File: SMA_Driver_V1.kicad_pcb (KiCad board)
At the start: 2 copper layers, 93 x 93 mm, 74 parts, among them J1 Human_Interface_Tether, J2 RM08V_Conn, Q1 Q_NMOS_GDS, Q2 Q_NMOS_GDS, U1 UDT020A0X3-SRZ, U2 INA332, U3 MCP3208, U4 MicroSD_Breakout_ADF

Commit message: fixed notes on 'SMA Driver V1 changes for V2'
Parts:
- Q1, Q2: footprint custom:SO-8FL -> custom:SO-8FL_v2
- moved TP6 19.6 mm to (79.4, 31.0)
- moved TP4 18.0 mm to (34.9, 31.0)
- moved TP15 7.52 mm to (62.9, 33.5)
- moved R3 6.88 mm to (57.1, 33.5)
- moved R8 6.69 mm to (54.6, 33.5)
- moved TP18 6.69 mm to (48.9, 33.5)
- moved Q1 1.69 mm to (69.2, 29.1), turned to 0 degrees
- moved Q2 1.53 mm to (42.5, 28.4), turned to 0 degrees
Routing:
- net /SMA1_G: track 18.5 -> 0.00 mm, vias 1 -> 0
- net /SMA2_G: track 10.1 -> 0.00 mm, vias 1 -> 0
- net GND: track 131.4 -> 122.9 mm
- net /SMA_COM2: track 67.8 -> 59.6 mm, vias 4 -> 2
- net /SMA_COM1: track 65.5 -> 58.3 mm
- net /V_SMA1_-: track 0.00 -> 1.19 mm
- net /V_SMA2_-: track 0.00 -> 0.51 mm
- removed copper zone on B.Cu, net /V_SMA1_-
- removed copper zone on B.Cu, net /V_SMA2_-

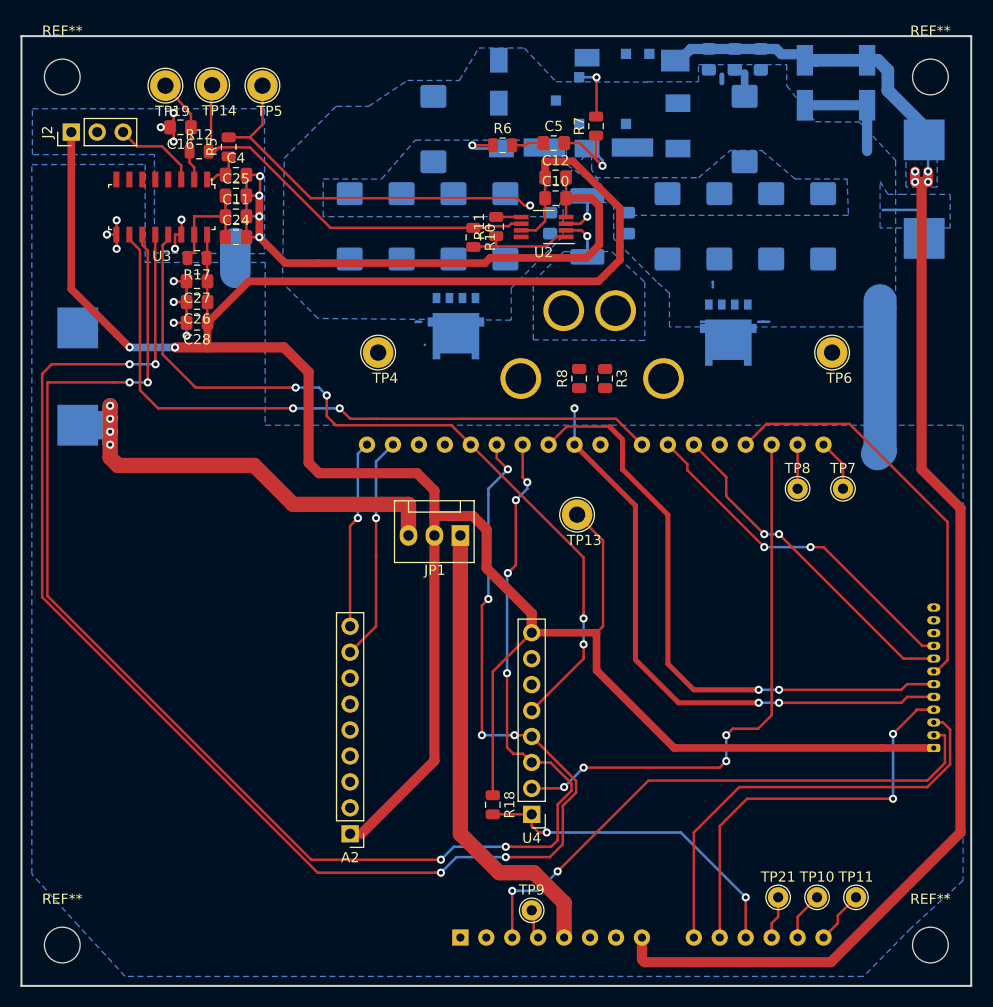
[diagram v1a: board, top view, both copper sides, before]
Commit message: PCB Rev 2.0 Fixed issues on PCB changes for V2 doc
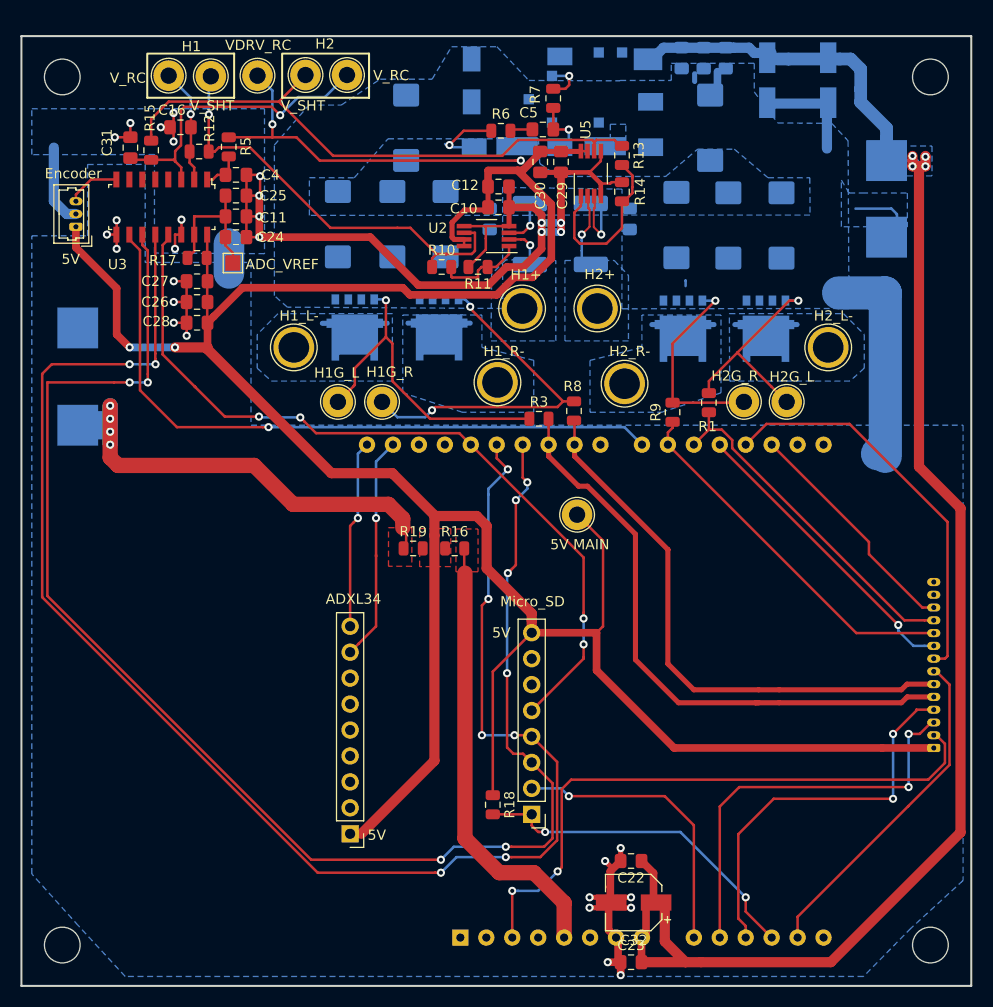
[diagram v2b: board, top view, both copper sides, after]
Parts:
- removed JP1: Jumper_NC_Dual, Connector:FanPinHeader_1x03_P2.54mm_Vertical
- removed TP9: 3V3, TestPoint:TestPoint_THTPad_D2.0mm_Drill1.0mm
- added C29: 100n, Capacitor_SMD:C_0805_2012Metric_Pad1.15x1.40mm_HandSolder, F.Cu at (52.8, 12.3)
- added C30: 4.7u, Capacitor_SMD:C_0805_2012Metric_Pad1.15x1.40mm_HandSolder, F.Cu at (50.8, 12.3)
- added C31: 1uF, Capacitor_SMD:C_0805_2012Metric_Pad1.15x1.40mm_HandSolder, F.Cu at (10.7, 10.9)
- added C32: 10uF, Capacitor_SMD:CP_Elec_5x5.3, F.Cu at (59.9, 84.8)
- added Q3: Q_NMOS_GDS, custom:SO-8FL_v2, B.Cu at (72.9, 28.7)
- added Q4: Q_NMOS_GDS, custom:SO-8FL_v2, B.Cu at (64.8, 28.7)
- added R1: 125, Resistor_SMD:R_0805_2012Metric, F.Cu at (67.3, 35.9)
- added R13: 24k, Resistor_SMD:R_0805_2012Metric, F.Cu at (58.8, 11.7)
- added R14: 1k, Resistor_SMD:R_0805_2012Metric, F.Cu at (58.8, 15.2)
- added R15: 30k, Resistor_SMD:R_0805_2012Metric, F.Cu at (12.7, 11.2)
- added R16: 0, Resistor_SMD:R_0805_2012Metric, F.Cu at (42.4, 50.2)
- added R19: 0, Resistor_SMD:R_0805_2012Metric, F.Cu at (38.4, 50.2)
- added R2: 4m, Resistor_SMD:R_2512_6332Metric_Pad1.52x3.35mm_HandSolder, B.Cu at (55.8, 19.4)
- added R9: 125, Resistor_SMD:R_0805_2012Metric, F.Cu at (63.8, 36.8)
- added TP20: I_SMA, TestPoint:TestPoint_Loop_D2.60mm_Drill1.6mm_Beaded, F.Cu at (27.8, 3.81)
- added TP22: VREF, TestPoint:TestPoint_Pad_1.5x1.5mm, F.Cu at (20.7, 22.2)
- added U5: INA332, Package_SO:VSSOP-8_3.0x3.0mm_P0.65mm, F.Cu at (55.8, 13.5)
- C22: value 330u -> 4.7u; footprint Capacitor_Tantalum_SMD:CP_EIA-7343-43_Kemet-X_Pad2.25x2.55mm_HandSolder -> Capacitor_SMD:C_0805_2012Metric_Pad1.15x1.40mm_HandSolder; moved to F.Cu
- C23: value 330u -> 100n; footprint Capacitor_Tantalum_SMD:CP_EIA-7343-43_Kemet-X_Pad2.25x2.55mm_HandSolder -> Capacitor_SMD:C_0805_2012Metric_Pad1.15x1.40mm_HandSolder; moved to F.Cu
- C5: value C -> 10n
- J1: footprint Connector_Molex:Molex_PicoBlade_53047-2410_1x12_P1.25mm_Vertical -> Connector_Molex:Molex_PicoBlade_53047-2810_1x14_P1.25mm_Vertical
- J2: footprint Connector_PinHeader_2.54mm:PinHeader_1x03_P2.54mm_Vertical -> Connector_Molex:Molex_PicoBlade_53047-0610_1x03_P1.25mm_Vertical
- R10: value R -> 24k
- R12: value 15.9k -> 30k
- R4: value 500u -> 4m
- R7: value C -> 15.8k
- TP10: value TestPoint -> SMA2+; footprint TestPoint:TestPoint_THTPad_D2.0mm_Drill1.0mm -> TestPoint:TestPoint_Plated_Hole_D3.0mm
- TP11: value TestPoint -> SMA2-; footprint TestPoint:TestPoint_THTPad_D2.0mm_Drill1.0mm -> TestPoint:TestPoint_Plated_Hole_D3.0mm
- TP15, TP16, TP18: moved to F.Cu
- TP17: value SMA2+ -> Gate_1; footprint TestPoint:TestPoint_Plated_Hole_D3.0mm -> TestPoint:TestPoint_Loop_D2.60mm_Drill1.6mm_Beaded; moved to F.Cu
- TP21: value TestPoint -> I_SMA_LP; footprint TestPoint:TestPoint_THTPad_D2.0mm_Drill1.0mm -> TestPoint:TestPoint_Loop_D2.60mm_Drill1.6mm_Beaded
- TP7: value TestPoint -> Gate_2; footprint TestPoint:TestPoint_THTPad_D2.0mm_Drill1.0mm -> TestPoint:TestPoint_Loop_D2.60mm_Drill1.6mm_Beaded
- TP8: value TestPoint -> SMA1-; footprint TestPoint:TestPoint_THTPad_D2.0mm_Drill1.0mm -> TestPoint:TestPoint_Plated_Hole_D3.0mm
- moved TP21 90.9 mm to (31.9, 3.81)
- moved C23 73.1 mm to (59.7, 90.7), turned to 0 degrees
- moved C22 64.5 mm to (59.7, 80.8), turned to 180 degrees
- moved TP10 61.5 mm to (56.4, 26.7)
- moved TP11 55.2 mm to (59.1, 34.0)
- moved TP6 48.6 mm to (31.0, 35.8)
- moved Q1 36.6 mm to (32.6, 28.6)
- moved TP15 36.3 mm to (26.7, 30.5), turned to 270 degrees
- moved C17 32.3 mm to (31.0, 18.4)
- moved TP17 15.4 mm to (70.7, 35.8)
- moved TP8 14.2 mm to (79.0, 30.5)
- moved TP7 10.1 mm to (74.9, 35.8)
- moved J2 9.28 mm to (5.33, 18.7)
- moved R3 7.58 mm to (50.7, 37.5), turned to 0 degrees
- moved C6 5.93 mm to (45.8, 17.9)
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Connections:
- net /Enc_CS renamed Net-(A1-Pad23)
- net /I_SEN_Amp renamed /I_SEN_Amp_1
- net /SMA1_G renamed /G_H1_R
- net /SMA2_G renamed /G_H1_L
- net /V_SHUNT renamed /V_SHUNT_1
- net /V_SMA1_- renamed /V_H1_R-
- net /V_SMA2_- renamed /V_H1_L-
- net /Vref renamed Net-(C11-Pad1)
- A1 pad 10: /POT_2 -> /POT_1
- A1 pad 11: /SD_CD -> /POT_2
- A1 pad 12: /A3 -> /SD_CD
- A1 pad 13: /A4 -> /LED_STAT_O
- A1 pad 14: /A5 -> Net-(A1-Pad14)
- A1 pad 15: /D0 -> Net-(A1-Pad15)
- A1 pad 16: /D1 -> Net-(A1-Pad16)
- A1 pad 17: /SD_CS -> /LED_STAT_P
- A1 pad 20: /LED_STAT_O1 -> /SMA_H2_L
- A1 pad 21: /LED_STAT_O2 -> /SMA_H2_R
- A1 pad 24: /SMA_COM1 -> /SMA_H1_R
- A1 pad 25: /SMA_COM2 -> /SMA_H1_L
- A1 pad 9: /POT_1 -> /SD_CS
- C22 pad 1: /I_SEN+ -> +12V
- C23 pad 1: /I_SEN+ -> GND
- C23 pad 2: GND -> +12V
- J1 pad 10: /LED_STAT_P1 -> /SMA_H2_R
- J1 pad 11: Net-(J1-Pad11) -> /SMA_H2_L
- J1 pad 12: GND -> /LED_STAT_P
- J1 pad 5: /SMA_COM1 -> /SMA_H1_L
- J1 pad 6: /SMA_COM2 -> /SMA_H1_R
- J1 pad 7: /LED_STAT_B1 -> /LED_STAT_O
- J1 pad 8: /LED_STAT_O1 -> /LED_STAT_B1
- J1 pad 9: /LED_STAT_O2 -> /LED_STAT_B2
- R11 pad 2: Net-(R11-Pad2) -> GND
- R3 pad 2: /SMA_COM2 -> /SMA_H1_L
- R4 pad 2: /I_SEN- -> /I_SEN1-
- R8 pad 1: /SMA_COM1 -> /SMA_H1_R
- TP10 pad 1: /A4 -> /I_SEN-
- TP11 pad 1: /A5 -> /V_H2_R-
- TP16 pad 1: /I_SEN- -> /I_SEN1-
- TP17 pad 1: /I_SEN- -> /G_H2_R
- TP21 pad 1: /A3 -> /V_SHUNT_2
- TP7 pad 1: /D0 -> /G_H2_L
- TP8 pad 1: /D1 -> /V_H2_L-
- U2 pad 2: /I_SEN- -> /I_SEN1-
- U2 pad 5: Net-(R11-Pad2) -> GND
- U2 pad 8: Net-(U2-Pad8) -> +5V
- U3 pad 3: /Enc_Vout -> /V_SHUNT_2
- U3 pad 8: Net-(U3-Pad8) -> /Enc_Vout
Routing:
- net GND: track 122.9 -> 190.7 mm, vias 16 -> 30
- net /SMA_COM2: track 59.6 -> 0.00 mm, vias 2 -> 0
- net /SMA_H1_L: track 0.00 -> 59.1 mm
- net /SMA_COM1: track 58.3 -> 0.00 mm, vias 3 -> 0
- net /I_SEN_Amp_2: track 0.00 -> 56.7 mm
- net /SMA_H1_R: track 0.00 -> 55.0 mm
- net /SMA_H2_R: track 0.00 -> 35.7 mm
- net /G_H1_R: track 0.00 -> 34.7 mm, vias 0 -> 2
- net /LED_STAT_O2: track 34.5 -> 0.00 mm, vias 2 -> 0
- net /SMA_H2_L: track 0.00 -> 34.1 mm
- net /LED_STAT_O1: track 33.3 -> 0.00 mm, vias 2 -> 0
- net /LED_STAT_O: track 0.00 -> 33.0 mm
- net /G_H1_L: track 0.00 -> 32.6 mm, vias 0 -> 1
- net /V_SHUNT_2: track 0.00 -> 30.2 mm, vias 0 -> 1
- net /LED_STAT_B2: track 0.00 -> 29.5 mm, vias 0 -> 1
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- added copper zone on F.Cu, net +5V
- added copper zone on F.Cu, net +5VP
- added copper zone on F.Cu, net /5V_Arduino
- added copper zone on B.Cu, net /I_SEN1-
- added copper zone on B.Cu, net /V_H1_L-
- added copper zone on B.Cu, net /V_H1_R-
- added copper zone on B.Cu, net /V_H2_L-
- added copper zone on B.Cu, net /V_H2_R-
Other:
- board text added: "+12V"
- board text added: "+5V EXT"
- board text added: "5V"
- board text added: "5V MAIN"
- board text added: "ADC_VREF"
- board text added: "ADXL34"
- board text added: "Encoder"
- board text added: "GND"
- board text added: "H1"
- board text added: "H1+"
- board text added: "H1G_L"
- board text added: "H1G_R"
- board text added: "H1_L-"
- board text added: "H1_R-"
- board text added: "H2"
- board text added: "H2+"
- board text added: "H2G_L"
- board text added: "H2G_R"
- board text added: "H2_L-"
- board text added: "H2_R-"
- board text added: "Micro_SD"
- board text added: "STAR Lab FLAPS V2.0"
- board text added: "VDRV_RC"
- board text added: "V_RC"
- board text added: "V_SHT"
- board text removed: "STAR Lab FLAPS V1.0 Charles Lindsay"

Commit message: added components for button, final draft 1
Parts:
- added R20: 10k, Resistor_SMD:R_0805_2012Metric, F.Cu at (80.0, 71.1)
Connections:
- A1 pad 14: Net-(A1-Pad14) -> /Button
- J1 pad 13: Net-(J1-Pad13) -> /LED_STAT_B1
- J1 pad 5: /SMA_H1_L -> /LED_STAT_O
- J1 pad 6: /SMA_H1_R -> /SMA_H1_L
- J1 pad 7: /LED_STAT_O -> /SMA_H1_R
- J1 pad 8: /LED_STAT_B1 -> /Button
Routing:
- net /Button: track 0.00 -> 35.0 mm, vias 0 -> 3
- net /LED_STAT_B1: track 39.2 -> 32.4 mm
- net /LED_STAT_O: track 33.0 -> 30.5 mm
- net +5V: track 260.0 -> 261.5 mm
- net /SMA_H1_R: track 55.0 -> 55.7 mm
- net /SMA_H1_L: track 59.1 -> 59.7 mm
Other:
- board text added: "CL"

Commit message: Final Board V2.0 after run DMC check completed with no errors
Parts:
- R1, R3, R8, R9: value 125 -> 124
- R5: value 15.9k -> 15.8k
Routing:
- net /I_SEN+: track 57.1 -> 56.0 mm
- net +5V: track 261.5 -> 260.7 mm
